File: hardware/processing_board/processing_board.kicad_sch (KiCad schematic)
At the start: 170 parts, among them IC1 XC7S25-2CSGA225I, J1 USB_C_Receptacle_USB2.0_14P, J2 USB_C_Receptacle_USB2.0_14P, J3 S2B-PH-K-S_LF__SN_, J4 Conn_02x07_Counter_Clockwise, SW1 SW_Push, SW2 BOOT_BTN, SW3 RST_BTN, U1 BQ24075RGT, U10 MAX98357A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

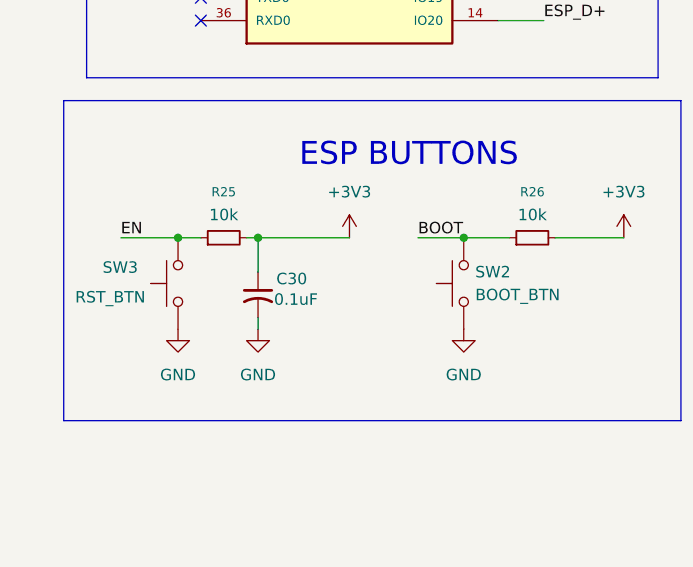
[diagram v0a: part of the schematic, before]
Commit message: Added BOOT and RST btns for ESP32, routed flash
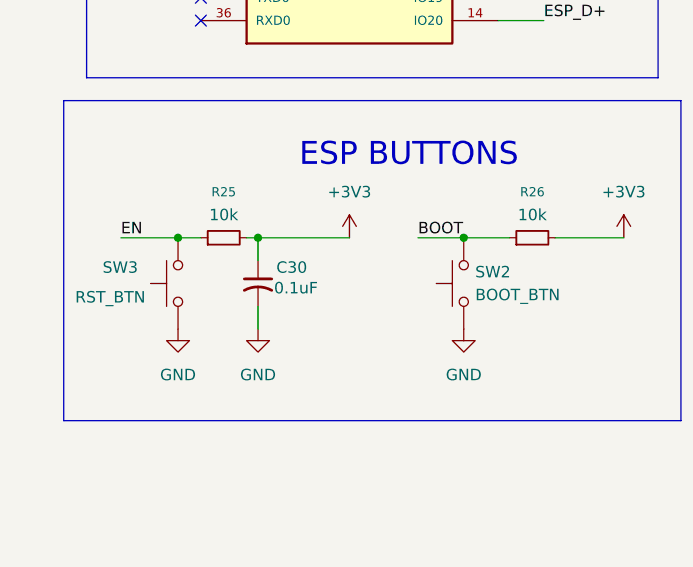
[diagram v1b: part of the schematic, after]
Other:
- moved on the sheet: C30
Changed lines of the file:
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@@
 	(wire
 		(pts
-			(xy 41.91 350.52) (xy 41.91 349.25)
+			(xy 41.91 350.52) (xy 41.91 347.98)
 		)
 		(stroke
@@
 	(wire
 		(pts
-			(xy 41.91 344.17) (xy 41.91 340.36)
+			(xy 41.91 342.9) (xy 41.91 340.36)
 		)
 		(stroke
@@
 	(symbol
 		(lib_id "Device:C_Small_US")
-		(at 41.91 346.71 0)
+		(at 41.91 345.44 0)
 		(unit 1)
 		(exclude_from_sim no)
@@
 		(dnp no)
 		(property "Reference" "C30"
-			(at 43.942 344.932 0)
+			(at 43.942 343.662 0)
 			(effects
 				(font
@@
 		)
 		(property "Value" "0.1uF"
-			(at 43.688 347.218 0)
+			(at 43.688 345.948 0)
 			(effects
 				(font
@@
 		)
 		(property "Footprint" "Capacitor_SMD:C_0402_1005Metric"
-			(at 41.91 346.71 0)
+			(at 41.91 345.44 0)
 			(effects
 				(font
@@
 		)
 		(property "Datasheet" ""
-			(at 41.91 346.71 0)
+			(at 41.91 345.44 0)
 			(effects
 				(font
@@
 		)
 		(property "Description" "capacitor, small US symbol"
-			(at 41.91 346.71 0)
+			(at 41.91 345.44 0)
 			(effects
 				(font

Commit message: Added routed USB-C to JTAG bridge
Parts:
- added C84: 0.1uF, Capacitor_SMD:C_0402_1005Metric, symbol Device:C_Small_US
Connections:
- net +3.3V: now also C84.1; no longer IC1.K5 (TMS_0)
- net GND: now also C84.2
- net TMS: now reaches R16.1, U6.19 (ADBUS3)
- net TMS: now also IC1.K5 (TMS_0)
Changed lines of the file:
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@@
 	(text "USB-C TO JTAG BRIDGE\n"
 		(exclude_from_sim no)
-		(at 283.21 90.424 0)
+		(at 283.21 89.154 0)
 		(effects
 			(font
@@
 	)
 	(junction
-		(at 326.39 119.38)
-		(diameter 0)
-		(color 0 0 0 0)
-	)
-	(junction
 		(at 373.38 350.52)
 		(diameter 0)
@@
 	)
 	(junction
+		(at 232.41 111.76)
+		(diameter 0)
+		(color 0 0 0 0)
+	)
+	(junction
 		(at 269.24 350.52)
 		(diameter 0)
@@
 	(wire
 		(pts
-			(xy 332.74 119.38) (xy 326.39 119.38)
-		)
-		(stroke
-			(width 0)
-			(type default)
-		)
-	)
-	(wire
-		(pts
 			(xy 102.87 281.94) (xy 111.76 281.94)
 		)
@@
 	(wire
 		(pts
-			(xy 250.19 111.76) (xy 252.73 111.76)
+			(xy 232.41 111.76) (xy 252.73 111.76)
 		)
 		(stroke
@@
 	(wire
 		(pts
+			(xy 227.33 111.76) (xy 232.41 111.76)
+		)
+		(stroke
+			(width 0)
+			(type default)
+		)
+	)
+	(wire
+		(pts
 			(xy 43.18 129.54) (xy 43.18 123.19)
 		)
@@
 		)
 	)
-	(label "TMS"
-		(at 332.74 119.38 0)
+	(label "VCCAUX"
+		(at 500.38 147.32 0)
 		(effects
 			(font
@@
 		)
 	)
-	(label "VCCAUX"
-		(at 500.38 147.32 0)
+	(label "VCCADC_0"
+		(at 391.16 246.38 0)
 		(effects
 			(font
@@
 		)
 	)
-	(label "VCCADC_0"
-		(at 391.16 246.38 0)
+	(label "TMS"
+		(at 313.69 119.38 0)
 		(effects
 			(font
@@
 	)
 	(symbol
+		(lib_id "power:GND")
+		(at 232.41 116.84 0)
+		(unit 1)
+		(exclude_from_sim no)
+		(in_bom yes)
+		(on_board yes)
+		(dnp no)
+		(fields_autoplaced yes)
+		(property "Reference" "#PWR0145"
+			(at 232.41 123.19 0)
+			(effects
+				(font
+					(size 1.27 1.27)
+				)
+				(hide yes)
+			)
+		)
+		(property "Value" "GND"
+			(at 232.41 121.92 0)
+			(effects
+				(font
+					(size 1.27 1.27)
+				)
+			)
+		)
+		(property "Footprint" ""
+			(at 232.41 116.84 0)
+			(effects
+				(font
+					(size 1.27 1.27)
+				)
+				(hide yes)
+			)
+		)
+		(property "Datasheet" ""
+			(at 232.41 116.84 0)
+			(effects
+				(font
+					(size 1.27 1.27)
+				)
+				(hide yes)
+			)
+		)
+		(property "Description" "Power symbol creates a global label with name \"GND\" , ground"
+			(at 232.41 116.84 0)
+			(effects
+				(font
+					(size 1.27 1.27)
+				)
+				(hide yes)
+			)
+		)
+		(pin "1"
+		)
+		(instances
+			(project ""
+				(path "/de118238-5cf0-4f20-b51d-7acba9897a1d"
+					(reference "#PWR0145")
+					(unit 1)
+				)
+			)
+		)
+	)
+	(symbol
 		(lib_id "Device:R_Small")
 		(at 233.68 39.37 0)
@@
 	(symbol
 		(lib_id "power:+3.3V")
-		(at 250.19 111.76 0)
+		(at 227.33 111.76 0)
 		(unit 1)
 		(exclude_from_sim no)
@@
 		(fields_autoplaced yes)
 		(property "Reference" "#PWR034"
-			(at 250.19 115.57 0)
+			(at 227.33 115.57 0)
 			(effects
 				(font
@@
 		)
 		(property "Value" "+3.3V"
-			(at 250.19 106.68 0)
+			(at 227.33 106.68 0)
 			(effects
 				(font
@@
 		)
 		(property "Footprint" ""
-			(at 250.19 111.76 0)
+			(at 227.33 111.76 0)
 			(effects
 				(font
@@
 		)
 		(property "Datasheet" ""
-			(at 250.19 111.76 0)
+			(at 227.33 111.76 0)
 			(effects
 				(font
@@
 		)
 		(property "Description" "Power symbol creates a global label with name \"+3.3V\""
-			(at 250.19 111.76 0)
+			(at 227.33 111.76 0)
 			(effects
 				(font
@@
 					(unit 1)
 				)
+			)
+		)
+	)
+	(symbol
+		(lib_id "Device:C_Small_US")
+		(at 232.41 114.3 0)
+		(unit 1)
+		(exclude_from_sim no)
+		(in_bom yes)
+		(on_board yes)
+		(dnp no)
+		(fields_autoplaced yes)
+		(property "Reference" "C84"
+			(at 234.95 113.1569 0)
+			(effects
+				(font
+					(size 1.27 1.27)
+				)
+				(justify left)
+			)
+		)
+		(property "Value" "0.1uF"
+			(at 234.95 115.6969 0)
+			(effects
+				(font
+					(size 1.27 1.27)
+				)
+				(justify left)
+			)
+		)
+		(property "Footprint" "Capacitor_SMD:C_0402_1005Metric"
+			(at 232.41 114.3 0)
+			(effects
+				(font
+					(size 1.27 1.27)
+				)
+				(hide yes)
+			)
+		)
+		(property "Datasheet" ""
+			(at 232.41 114.3 0)
+			(effects
+				(font
+					(size 1.27 1.27)
+				)
+				(hide yes)
+			)
+		)
+		(property "Description" "capacitor, small US symbol"
+			(at 232.41 114.3 0)
+			(effects
+				(font
+					(size 1.27 1.27)
+				)
+				(hide yes)
+			)
+		)
+		(pin "1"
+		)
+		(pin "2"
+		)
+		(instances
+			(project ""
+				(path "/de118238-5cf0-4f20-b51d-7acba9897a1d"
+					(reference "C84")
+					(unit 1)
+				)
